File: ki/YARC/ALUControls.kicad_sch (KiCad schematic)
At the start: 11 parts, among them U123 74LS32, U124 74LS08, U125 74LS08, U126 74LS08, U127 74LS74, U129 74LS574, U130 74LS157, U131 74LS245, U136 74LS32, U137 74HC00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

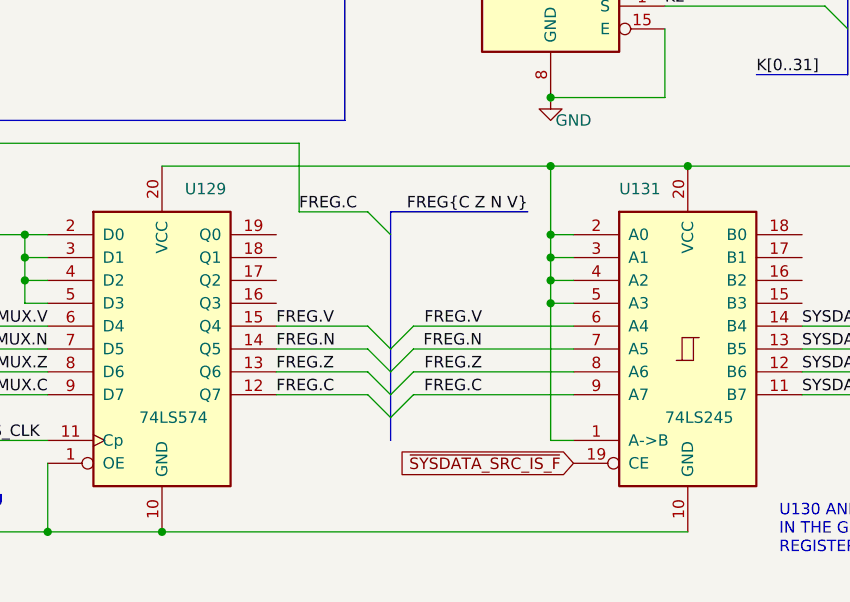
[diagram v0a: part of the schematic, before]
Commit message: Removed about 2/3 of 2300+ errors from the ERC
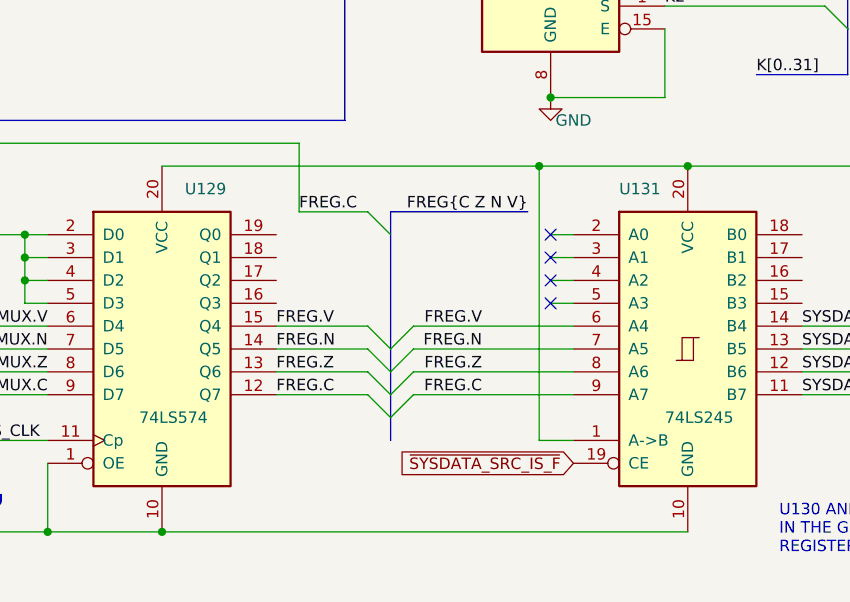
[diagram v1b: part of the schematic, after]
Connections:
- net VCC: no longer U131.2 (A0), U131.3 (A1), U131.4 (A2), U131.5 (A3)
- no-connect marks 0 -> 4
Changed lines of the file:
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@@
   (junction (at 195.58 167.64) (diameter 0) (color 0 0 0 0)
   )
-  (junction (at 210.82 101.6) (diameter 0) (color 0 0 0 0)
-  )
   (junction (at 167.64 167.64) (diameter 0) (color 0 0 0 0)
   )
@@
   (junction (at 167.64 132.08) (diameter 0) (color 0 0 0 0)
   )
-  (junction (at 210.82 106.68) (diameter 0) (color 0 0 0 0)
-  )
   (junction (at 129.54 193.04) (diameter 0) (color 0 0 0 0)
   )
@@
   (junction (at 154.94 132.08) (diameter 0) (color 0 0 0 0)
   )
-  (junction (at 210.82 104.14) (diameter 0) (color 0 0 0 0)
+  (junction (at 209.55 91.44) (diameter 0) (color 0 0 0 0)
   )
   (junction (at 91.44 138.43) (diameter 0) (color 0 0 0 0)
@@
   (junction (at 210.82 83.82) (diameter 0) (color 0 0 0 0)
   )
-  (junction (at 210.82 91.44) (diameter 0) (color 0 0 0 0)
-  )
   (junction (at 208.28 167.64) (diameter 0) (color 0 0 0 0)
   )
@@
   (junction (at 129.54 180.34) (diameter 0) (color 0 0 0 0)
   )
-  (junction (at 210.82 99.06) (diameter 0) (color 0 0 0 0)
-  )
   (junction (at 152.4 104.14) (diameter 0) (color 0 0 0 0)
   )
@@
   (junction (at 246.38 142.24) (diameter 0) (color 0 0 0 0)
   )
+  (no_connect (at 210.82 99.06))
+  (no_connect (at 210.82 101.6))
+  (no_connect (at 210.82 106.68))
+  (no_connect (at 210.82 104.14))
   (bus_entry (at 187.96 60.96) (size 2.54 -2.54)
     (stroke (width 0) (type default))
@@
     (stroke (width 0) (type default))
   )
-  (wire (pts (xy 210.82 121.92) (xy 210.82 106.68))
-    (stroke (width 0) (type default))
-  )
   (wire (pts (xy 190.5 116.84) (xy 180.34 116.84))
     (stroke (width 0) (type default))
@@
     (stroke (width 0) (type default))
   )
-  (wire (pts (xy 210.82 106.68) (xy 210.82 104.14))
-    (stroke (width 0) (type default))
-  )
   (wire (pts (xy 99.06 22.86) (xy 88.9 22.86))
     (stroke (width 0) (type default))
@@
     (stroke (width 0) (type default))
   )
-  (wire (pts (xy 210.82 91.44) (xy 226.06 91.44))
+  (wire (pts (xy 167.64 91.44) (xy 209.55 91.44))
     (stroke (width 0) (type default))
   )
@@
     (stroke (width 0) (type default))
   )
-  (wire (pts (xy 213.36 121.92) (xy 210.82 121.92))
-    (stroke (width 0) (type default))
-  )
   (wire (pts (xy 48.26 50.8) (xy 50.8 50.8))
     (stroke (width 0) (type default))
@@
     (stroke (width 0) (type default))
   )
-  (wire (pts (xy 210.82 104.14) (xy 210.82 101.6))
-    (stroke (width 0) (type default))
-  )
   (wire (pts (xy 91.44 135.89) (xy 91.44 138.43))
     (stroke (width 0) (type default))
@@
     (stroke (width 0) (type default))
   )
+  (wire (pts (xy 209.55 121.92) (xy 213.36 121.92))
+    (stroke (width 0) (type default))
+  )
   (wire (pts (xy 129.54 167.64) (xy 167.64 167.64))
     (stroke (width 0) (type default))
@@
     (stroke (width 0) (type default))
   )
-  (wire (pts (xy 210.82 91.44) (xy 167.64 91.44))
-    (stroke (width 0) (type default))
-  )
   (bus (pts (xy 25.4 93.98) (xy 25.4 106.68))
     (stroke (width 0) (type default))
@@
     (stroke (width 0) (type default))
   )
-  (wire (pts (xy 210.82 101.6) (xy 210.82 99.06))
-    (stroke (width 0) (type default))
-  )
   (wire (pts (xy 45.72 81.28) (xy 45.72 68.58))
     (stroke (width 0) (type default))
@@
     (stroke (width 0) (type default))
   )
+  (wire (pts (xy 209.55 91.44) (xy 226.06 91.44))
+    (stroke (width 0) (type default))
+  )
   (wire (pts (xy 226.06 91.44) (xy 259.08 91.44))
     (stroke (width 0) (type default))
@@
     (stroke (width 0) (type default))
   )
+  (wire (pts (xy 209.55 91.44) (xy 209.55 121.92))
+    (stroke (width 0) (type default))
+  )
   (bus (pts (xy 243.84 71.12) (xy 243.84 76.2))
     (stroke (width 0) (type default))
@@
     (stroke (width 0) (type default))
   )
-  (wire (pts (xy 210.82 99.06) (xy 210.82 91.44))
-    (stroke (width 0) (type default))
-  )

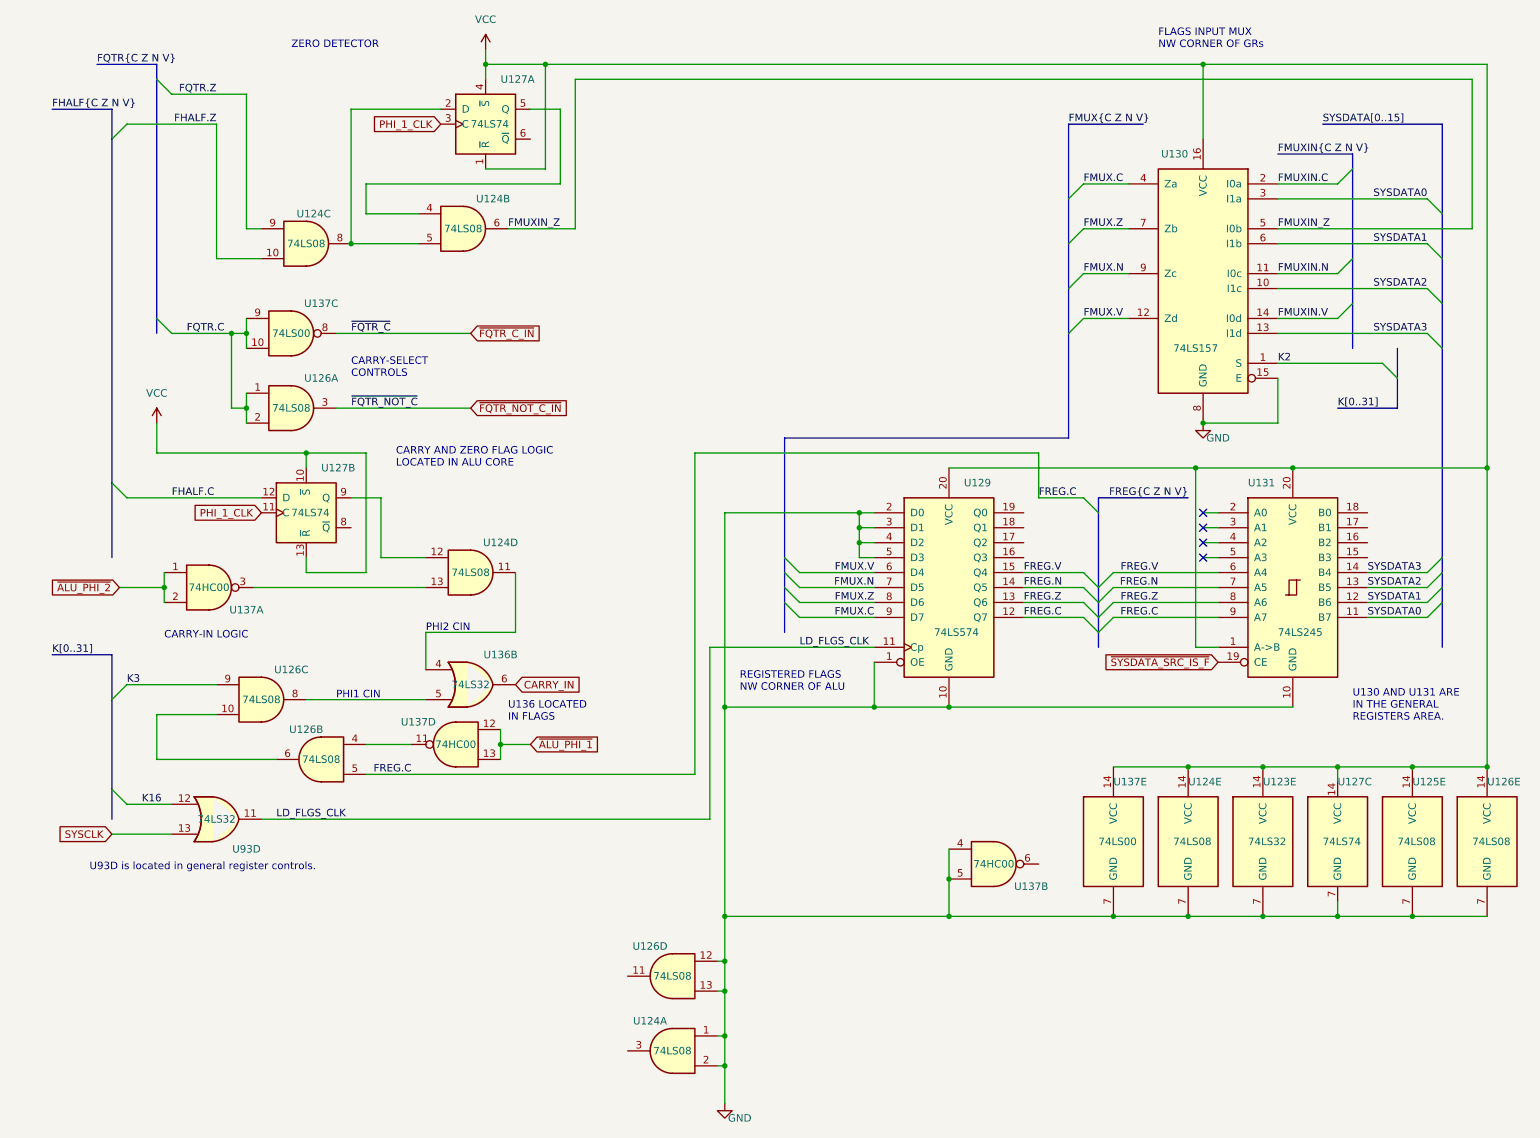
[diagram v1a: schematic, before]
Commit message: Ongoing fixes for ERC errors
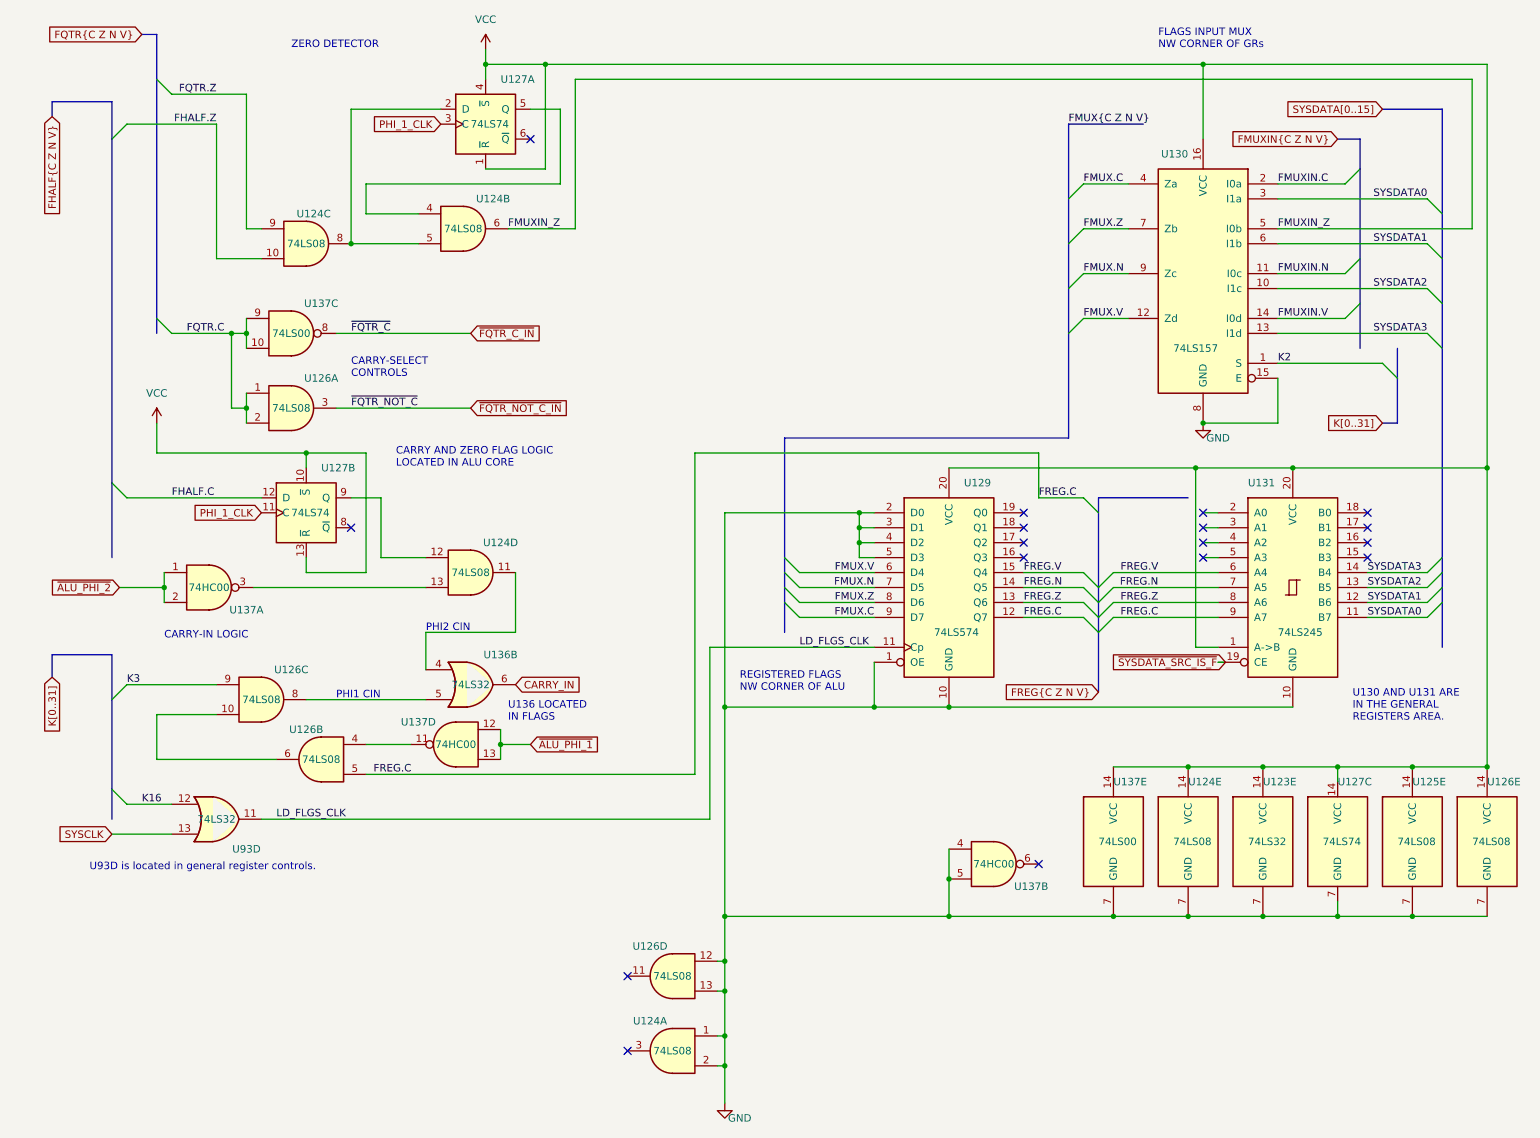
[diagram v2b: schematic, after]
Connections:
- no-connect marks 4 -> 17

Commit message: Schematic for addressing unit is complete and all ERC violations addressed
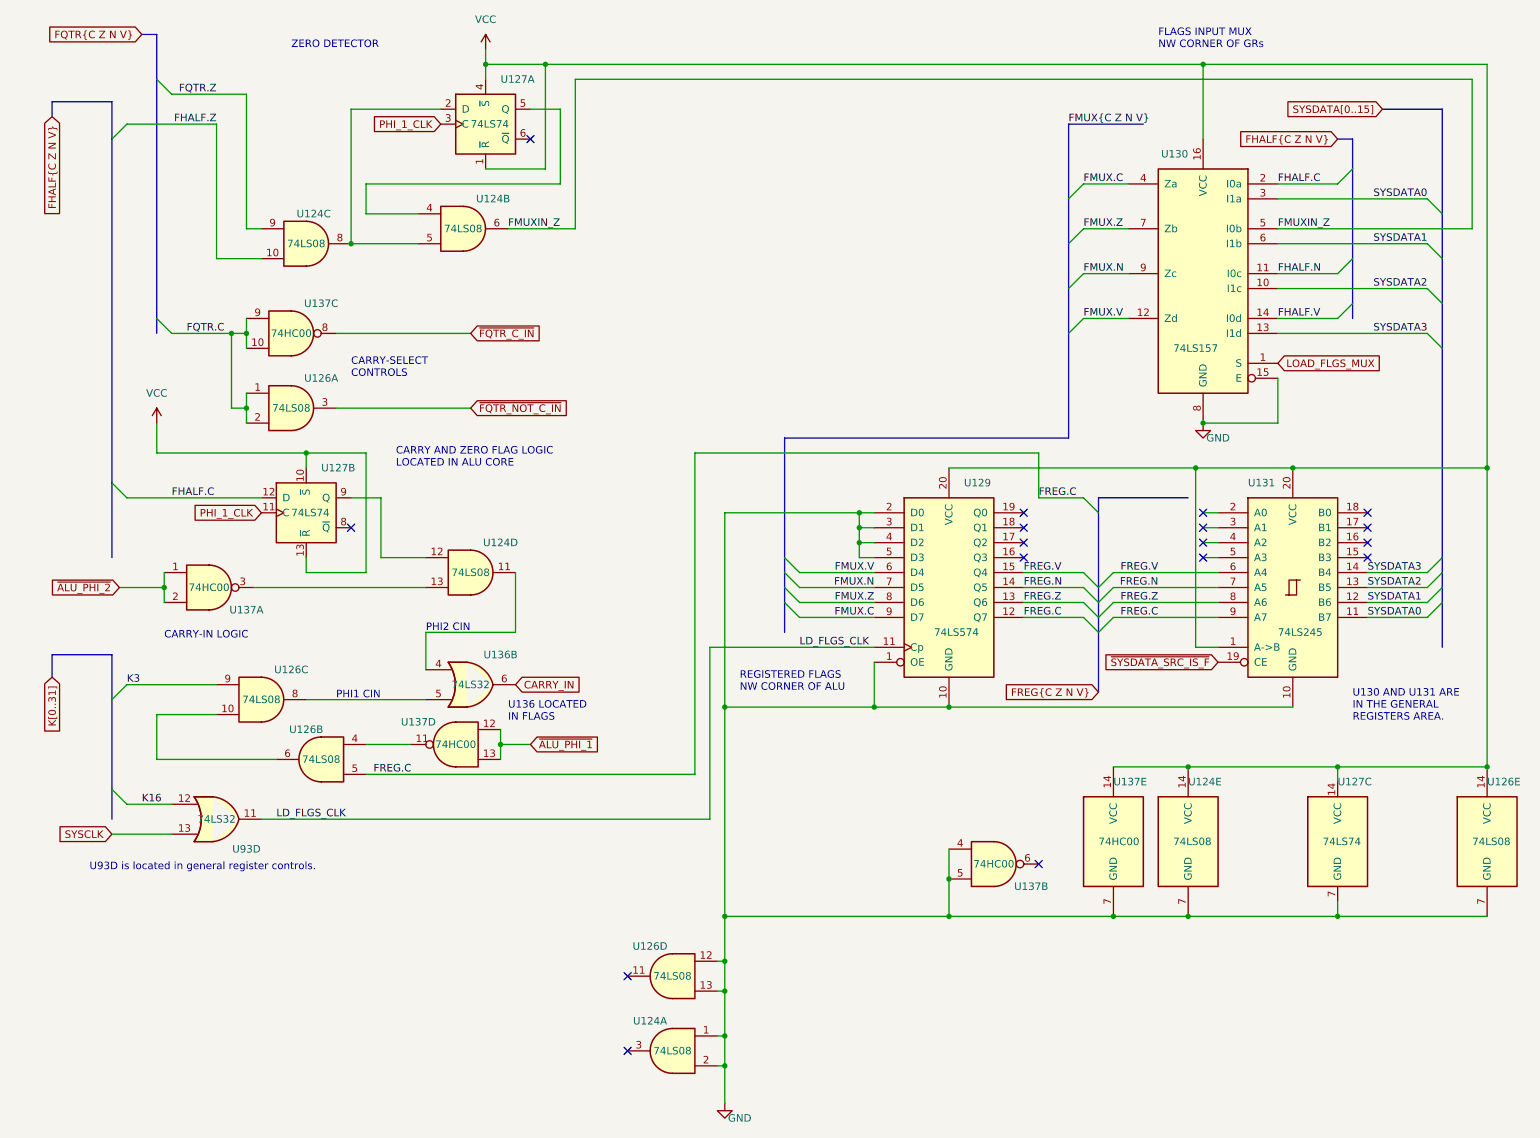
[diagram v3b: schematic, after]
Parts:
- removed U123: 74LS32, symbol 74xx:74LS32
- removed U125: 74LS08, symbol 74xx:74LS08
- U137: value 74LS00 -> 74HC00
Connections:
- net FMUXIN.C is gone; now on net FHALF.C: U130.2 (I0a)
- net FMUXIN.N renamed FHALF.N
- net FMUXIN.V renamed FHALF.V
- net K2 renamed LOAD_FLGS_MUX
